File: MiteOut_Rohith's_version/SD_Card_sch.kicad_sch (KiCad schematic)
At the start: 2 parts, among them J3 SD_Card_Receptacle, U2 4050

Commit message: SD Card edits
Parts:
- added U10, U3, U4, U8, U9: 4050, symbol 4xxx:4050
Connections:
- net at U2.2: now also J3.5 (CLK)
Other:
- moved on the sheet: U2A

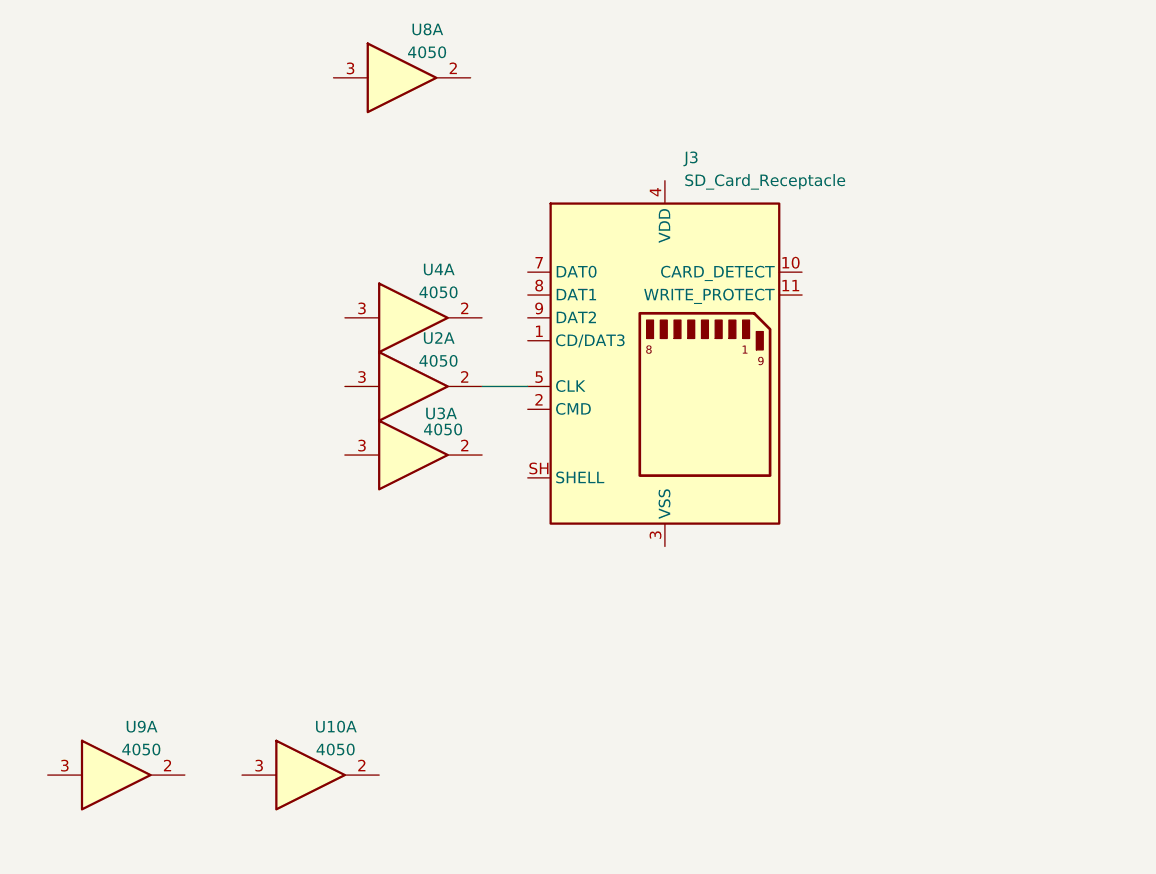
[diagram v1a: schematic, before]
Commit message: Finished MicroSD
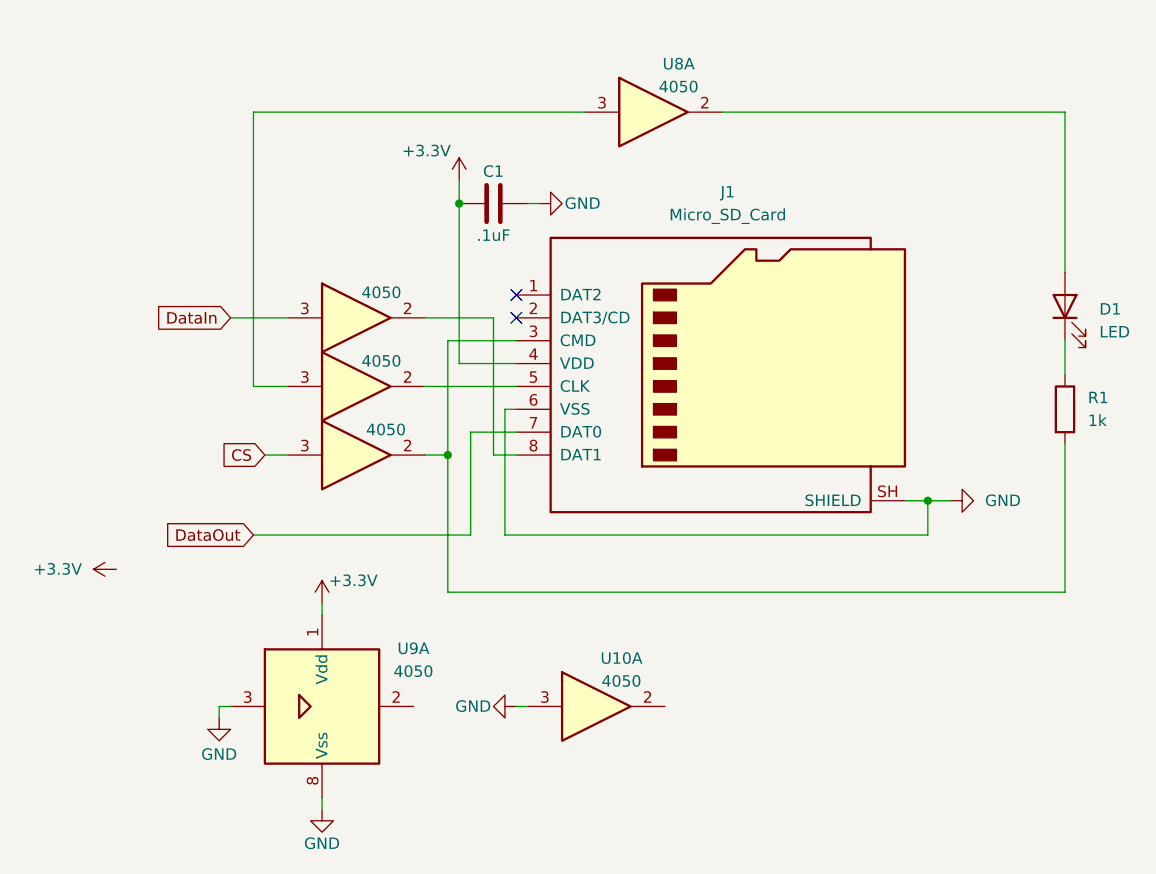
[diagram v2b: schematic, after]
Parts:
- removed J3: SD_Card_Receptacle, symbol Connector:SD_Card_Receptacle
- removed U9: 4050, symbol 4xxx:4050
- added C1: .1uF, symbol Device:C
- added D1: LED, symbol Device:LED
- added J1: Micro_SD_Card, symbol Connector:Micro_SD_Card
- added R1: 1k, symbol Device:R
- added U9: 4050, symbol 4xxx_IEEE:4050
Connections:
- net at U8.2: now also D1.2 (A)
- net at U8.3: now also U2.3
- net at U4.2: now also J1.8 (DAT1)
- net DataIn: now reaches U4.3
- net at U2.2: now also J1.5 (CLK)
- net GND: now reaches U10.3
- net GND: now also C1.2, J1.6 (VSS), J1.SH (SHIELD), U9.3, U9.8 (Vss)
- net at U3.2: now also J1.3 (CMD), R1.2
- net CS: now reaches U3.3
- new net: D1.1 (K), R1.1
- new net +3.3V: C1.1, J1.4 (VDD), U9.1 (Vdd)
- new net DataOut: J1.7 (DAT0)
- no-connect marks 0 -> 2
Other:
- moved on the sheet: U10A, U8A

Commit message: Full Schematic Draft 1
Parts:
- added U12: LP2985-3.3, Package_TO_SOT_SMD:SOT-23-5, symbol Regulator_Linear:LP2985-3.3
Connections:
- net +3.3V: now also U12.5 (VOUT)
- net GND: now also U12.2 (GND)
- net CLK: now reaches U2.3, U8.3
- new net VCC: U12.1 (VIN), U12.3 (ON/~{OFF})
- no-connect marks 2 -> 3

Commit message: some error fixes
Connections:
- no-connect marks 3 -> 5
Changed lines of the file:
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@@
+	)
+	(no_connect
+		(at 100.33 121.92)
 	)
 	(no_connect
@@
 		(at 162.56 124.46)
 	)
+	(no_connect
+		(at 128.27 121.92)
+	)
 	(wire
 		(pts
@@
 	(wire
 		(pts
-			(xy 106.68 102.87) (xy 82.55 102.87)
-		)
-		(stroke
-			(width 0)
-			(type default)
-		)
-	)
-	(wire
-		(pts
-			(xy 80.01 78.74) (xy 86.36 78.74)
+			(xy 106.68 102.87) (xy 81.28 102.87)
+		)
+		(stroke
+			(width 0)
+			(type default)
+		)
+	)
+	(wire
+		(pts
+			(xy 81.28 78.74) (xy 86.36 78.74)
 		)
 		(stroke
@@
 	(wire
 		(pts
-			(xy 83.82 93.98) (xy 86.36 93.98)
+			(xy 81.28 93.98) (xy 86.36 93.98)
 		)
 		(stroke
@@
 	(hierarchical_label "DataIn"
 		(shape input)
-		(at 80.01 78.74 180)
+		(at 81.28 78.74 180)
 		(effects
 			(font
@@
 	(hierarchical_label "CS"
 		(shape input)
-		(at 83.82 93.98 180)
+		(at 81.28 93.98 180)
 		(effects
 			(font
@@
 	(hierarchical_label "DataOut"
 		(shape input)
-		(at 82.55 102.87 180)
+		(at 81.28 102.87 180)
 		(effects
 			(font

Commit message: Fully checked schematic
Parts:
- removed C1: .1uF, symbol Device:C
- added C21: .1uF, symbol Device:C
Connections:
- net +3.3V: now also C21.1
- net GND: now also C21.2
- net VCC renamed +5V
